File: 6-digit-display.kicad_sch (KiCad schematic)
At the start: 5 parts, among them U2 MAX7219, U3 6_digit_7_segment_display_1

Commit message: More footprint updates
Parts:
- U9: renamed from U3; footprint Generic-radio-stack:6 digit (3x2) 7 segment LED display -> Generic-radio-stack:6 digit (3+3) 7 segment LED display
- renumbered C4 to C10, C3 to C9, R10 to R13, U2 to U8
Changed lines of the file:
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@@
   (symbol (lib_id "Driver_LED:MAX7219") (at 60.96 101.6 0)
     (in_bom yes) (on_board yes) (fields_autoplaced)
-    (property "Reference" "U2" (id 0) (at 62.9794 73.66 0)
+    (property "Reference" "U8" (id 0) (at 62.9794 73.66 0)
       (effects (font (size 1.27 1.27)) (justify left))
     )
@@
   (symbol (lib_id "Device:C_Small") (at 38.1 78.74 0)
     (in_bom yes) (on_board yes) (fields_autoplaced)
-    (property "Reference" "C4" (id 0) (at 40.64 77.4762 0)
+    (property "Reference" "C10" (id 0) (at 40.64 77.4762 0)
       (effects (font (size 1.27 1.27)) (justify left))
     )
@@
   (symbol (lib_id "power:GND") (at 38.1 81.28 0)
     (in_bom yes) (on_board yes) (fields_autoplaced)
-    (property "Reference" "#PWR013" (id 0) (at 38.1 87.63 0)
+    (property "Reference" "#PWR025" (id 0) (at 38.1 87.63 0)
       (effects (font (size 1.27 1.27)) hide)
     )
@@
   (symbol (lib_id "Device:R_Small") (at 48.26 87.63 0)
     (in_bom yes) (on_board yes)
-    (property "Reference" "R10" (id 0) (at 46.99 86.36 0)
+    (property "Reference" "R13" (id 0) (at 46.99 86.36 0)
       (effects (font (size 1.27 1.27)) (justify right))
     )
@@
   (symbol (lib_id "power:+5V") (at 38.1 76.2 0)
     (in_bom yes) (on_board yes) (fields_autoplaced)
-    (property "Reference" "#PWR012" (id 0) (at 38.1 80.01 0)
+    (property "Reference" "#PWR024" (id 0) (at 38.1 80.01 0)
       (effects (font (size 1.27 1.27)) hide)
     )
@@
   (symbol (lib_id "power:GND") (at 48.26 90.17 0)
     (in_bom yes) (on_board yes) (fields_autoplaced)
-    (property "Reference" "#PWR014" (id 0) (at 48.26 96.52 0)
+    (property "Reference" "#PWR026" (id 0) (at 48.26 96.52 0)
       (effects (font (size 1.27 1.27)) hide)
     )
@@
   (symbol (lib_id "power:GND") (at 60.96 127 0)
     (in_bom yes) (on_board yes) (fields_autoplaced)
-    (property "Reference" "#PWR015" (id 0) (at 60.96 133.35 0)
+    (property "Reference" "#PWR027" (id 0) (at 60.96 133.35 0)
       (effects (font (size 1.27 1.27)) hide)
     )
@@
   (symbol (lib_id "Generic-radio-stack:6_digit_7_segment_display_1") (at 113.03 90.17 0)
     (in_bom yes) (on_board yes) (fields_autoplaced)
-    (property "Reference" "U3" (id 0) (at 114.3 74.93 0))
+    (property "Reference" "U9" (id 0) (at 114.3 74.93 0))
     (property "Value" "6_digit_7_segment_display_1" (id 1) (at 114.3 77.47 0))
-    (property "Footprint" "Generic-radio-stack:6 digit (3x2) 7 segment LED display" (id 2) (at 113.03 104.775 0)
+    (property "Footprint" "Generic-radio-stack:6 digit (3+3) 7 segment LED display" (id 2) (at 113.03 104.775 0)
       (effects (font (size 1.27 1.27)) hide)
     )
@@
   (symbol (lib_id "Device:C_Small") (at 27.94 78.74 0)
     (in_bom yes) (on_board yes) (fields_autoplaced)
-    (property "Reference" "C3" (id 0) (at 30.48 77.4762 0)
+    (property "Reference" "C9" (id 0) (at 30.48 77.4762 0)
       (effects (font (size 1.27 1.27)) (justify left))
     )

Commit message: Board layout begins. Ugh.
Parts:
- renumbered C9 to C7, C10 to C8, R13 to R12, U8 to U6, U9 to U7
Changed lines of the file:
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@@
   (symbol (lib_id "Driver_LED:MAX7219") (at 60.96 101.6 0)
     (in_bom yes) (on_board yes) (fields_autoplaced)
-    (property "Reference" "U8" (id 0) (at 62.9794 73.66 0)
+    (property "Reference" "U6" (id 0) (at 62.9794 73.66 0)
       (effects (font (size 1.27 1.27)) (justify left))
     )
@@
   (symbol (lib_id "Device:C_Small") (at 38.1 78.74 0)
     (in_bom yes) (on_board yes) (fields_autoplaced)
-    (property "Reference" "C10" (id 0) (at 40.64 77.4762 0)
+    (property "Reference" "C8" (id 0) (at 40.64 77.4762 0)
       (effects (font (size 1.27 1.27)) (justify left))
     )
@@
   (symbol (lib_id "power:GND") (at 38.1 81.28 0)
     (in_bom yes) (on_board yes) (fields_autoplaced)
-    (property "Reference" "#PWR025" (id 0) (at 38.1 87.63 0)
+    (property "Reference" "#PWR021" (id 0) (at 38.1 87.63 0)
       (effects (font (size 1.27 1.27)) hide)
     )
@@
   (symbol (lib_id "Device:R_Small") (at 48.26 87.63 0)
     (in_bom yes) (on_board yes)
-    (property "Reference" "R13" (id 0) (at 46.99 86.36 0)
+    (property "Reference" "R12" (id 0) (at 46.99 86.36 0)
       (effects (font (size 1.27 1.27)) (justify right))
     )
@@
   (symbol (lib_id "power:+5V") (at 38.1 76.2 0)
     (in_bom yes) (on_board yes) (fields_autoplaced)
-    (property "Reference" "#PWR024" (id 0) (at 38.1 80.01 0)
+    (property "Reference" "#PWR020" (id 0) (at 38.1 80.01 0)
       (effects (font (size 1.27 1.27)) hide)
     )
@@
   (symbol (lib_id "power:GND") (at 48.26 90.17 0)
     (in_bom yes) (on_board yes) (fields_autoplaced)
-    (property "Reference" "#PWR026" (id 0) (at 48.26 96.52 0)
+    (property "Reference" "#PWR022" (id 0) (at 48.26 96.52 0)
       (effects (font (size 1.27 1.27)) hide)
     )
@@
   (symbol (lib_id "power:GND") (at 60.96 127 0)
     (in_bom yes) (on_board yes) (fields_autoplaced)
-    (property "Reference" "#PWR027" (id 0) (at 60.96 133.35 0)
+    (property "Reference" "#PWR023" (id 0) (at 60.96 133.35 0)
       (effects (font (size 1.27 1.27)) hide)
     )
@@
   (symbol (lib_id "Generic-radio-stack:6_digit_7_segment_display_1") (at 113.03 90.17 0)
     (in_bom yes) (on_board yes) (fields_autoplaced)
-    (property "Reference" "U9" (id 0) (at 114.3 74.93 0))
+    (property "Reference" "U7" (id 0) (at 114.3 74.93 0))
     (property "Value" "6_digit_7_segment_display_1" (id 1) (at 114.3 77.47 0))
     (property "Footprint" "Generic-radio-stack:6 digit (3+3) 7 segment LED display" (id 2) (at 113.03 104.775 0)
@@
   (symbol (lib_id "Device:C_Small") (at 27.94 78.74 0)
     (in_bom yes) (on_board yes) (fields_autoplaced)
-    (property "Reference" "C9" (id 0) (at 30.48 77.4762 0)
+    (property "Reference" "C7" (id 0) (at 30.48 77.4762 0)
       (effects (font (size 1.27 1.27)) (justify left))
     )

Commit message: Added dual encoder 3d model, fit everything on the board
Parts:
- renumbered C8 to C10, C7 to C9, R12 to R13, U7 to U10, U6 to U9
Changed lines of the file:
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@@
   (symbol (lib_id "Driver_LED:MAX7219") (at 60.96 101.6 0)
     (in_bom yes) (on_board yes) (fields_autoplaced)
-    (property "Reference" "U6" (id 0) (at 62.9794 73.66 0)
+    (property "Reference" "U9" (id 0) (at 62.9794 73.66 0)
       (effects (font (size 1.27 1.27)) (justify left))
     )
@@
   (symbol (lib_id "Device:C_Small") (at 38.1 78.74 0)
     (in_bom yes) (on_board yes) (fields_autoplaced)
-    (property "Reference" "C8" (id 0) (at 40.64 77.4762 0)
+    (property "Reference" "C10" (id 0) (at 40.64 77.4762 0)
       (effects (font (size 1.27 1.27)) (justify left))
     )
@@
   (symbol (lib_id "power:GND") (at 38.1 81.28 0)
     (in_bom yes) (on_board yes) (fields_autoplaced)
-    (property "Reference" "#PWR021" (id 0) (at 38.1 87.63 0)
+    (property "Reference" "#PWR027" (id 0) (at 38.1 87.63 0)
       (effects (font (size 1.27 1.27)) hide)
     )
@@
   (symbol (lib_id "Device:R_Small") (at 48.26 87.63 0)
     (in_bom yes) (on_board yes)
-    (property "Reference" "R12" (id 0) (at 46.99 86.36 0)
+    (property "Reference" "R13" (id 0) (at 46.99 86.36 0)
       (effects (font (size 1.27 1.27)) (justify right))
     )
@@
   (symbol (lib_id "power:+5V") (at 38.1 76.2 0)
     (in_bom yes) (on_board yes) (fields_autoplaced)
-    (property "Reference" "#PWR020" (id 0) (at 38.1 80.01 0)
+    (property "Reference" "#PWR026" (id 0) (at 38.1 80.01 0)
       (effects (font (size 1.27 1.27)) hide)
     )
@@
   (symbol (lib_id "power:GND") (at 48.26 90.17 0)
     (in_bom yes) (on_board yes) (fields_autoplaced)
-    (property "Reference" "#PWR022" (id 0) (at 48.26 96.52 0)
+    (property "Reference" "#PWR028" (id 0) (at 48.26 96.52 0)
       (effects (font (size 1.27 1.27)) hide)
     )
@@
   (symbol (lib_id "power:GND") (at 60.96 127 0)
     (in_bom yes) (on_board yes) (fields_autoplaced)
-    (property "Reference" "#PWR023" (id 0) (at 60.96 133.35 0)
+    (property "Reference" "#PWR029" (id 0) (at 60.96 133.35 0)
       (effects (font (size 1.27 1.27)) hide)
     )
@@
   (symbol (lib_id "Generic-radio-stack:6_digit_7_segment_display_1") (at 113.03 90.17 0)
     (in_bom yes) (on_board yes) (fields_autoplaced)
-    (property "Reference" "U7" (id 0) (at 114.3 74.93 0))
+    (property "Reference" "U10" (id 0) (at 114.3 74.93 0))
     (property "Value" "6_digit_7_segment_display_1" (id 1) (at 114.3 77.47 0))
     (property "Footprint" "Generic-radio-stack:6 digit (3+3) 7 segment LED display" (id 2) (at 113.03 104.775 0)
@@
   (symbol (lib_id "Device:C_Small") (at 27.94 78.74 0)
     (in_bom yes) (on_board yes) (fields_autoplaced)
-    (property "Reference" "C7" (id 0) (at 30.48 77.4762 0)
+    (property "Reference" "C9" (id 0) (at 30.48 77.4762 0)
       (effects (font (size 1.27 1.27)) (justify left))
     )

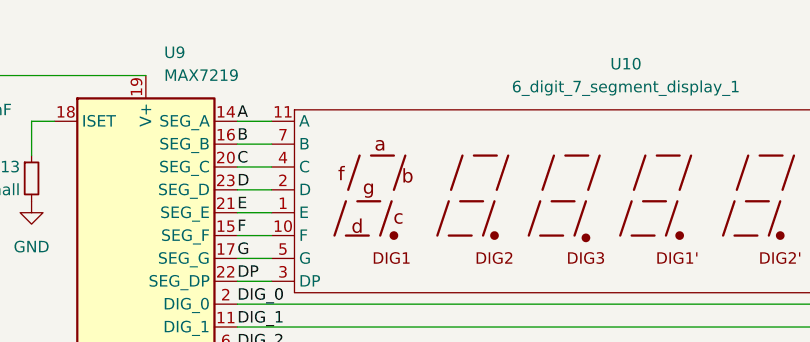
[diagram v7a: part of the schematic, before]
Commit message: Add mounting holes
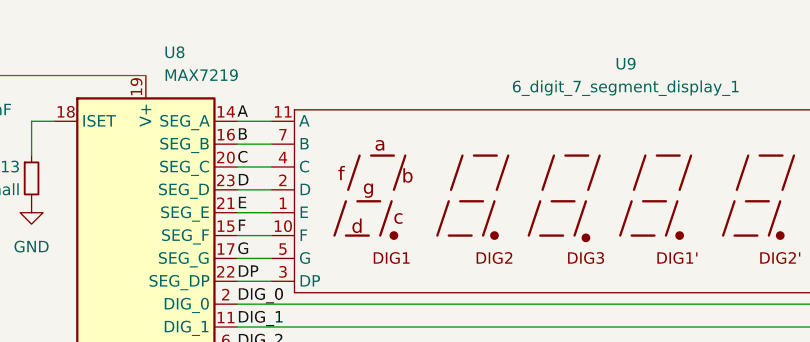
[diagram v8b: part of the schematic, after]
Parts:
- renumbered U9 to U8, U10 to U9
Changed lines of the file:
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@@
   (symbol (lib_id "Driver_LED:MAX7219") (at 60.96 101.6 0)
     (in_bom yes) (on_board yes) (fields_autoplaced)
-    (property "Reference" "U9" (id 0) (at 62.9794 73.66 0)
+    (property "Reference" "U8" (id 0) (at 62.9794 73.66 0)
       (effects (font (size 1.27 1.27)) (justify left))
     )
@@
   (symbol (lib_id "power:GND") (at 38.1 81.28 0)
     (in_bom yes) (on_board yes) (fields_autoplaced)
-    (property "Reference" "#PWR027" (id 0) (at 38.1 87.63 0)
+    (property "Reference" "#PWR025" (id 0) (at 38.1 87.63 0)
       (effects (font (size 1.27 1.27)) hide)
     )
@@
   (symbol (lib_id "power:+5V") (at 38.1 76.2 0)
     (in_bom yes) (on_board yes) (fields_autoplaced)
-    (property "Reference" "#PWR026" (id 0) (at 38.1 80.01 0)
+    (property "Reference" "#PWR024" (id 0) (at 38.1 80.01 0)
       (effects (font (size 1.27 1.27)) hide)
     )
@@
   (symbol (lib_id "power:GND") (at 48.26 90.17 0)
     (in_bom yes) (on_board yes) (fields_autoplaced)
-    (property "Reference" "#PWR028" (id 0) (at 48.26 96.52 0)
+    (property "Reference" "#PWR026" (id 0) (at 48.26 96.52 0)
       (effects (font (size 1.27 1.27)) hide)
     )
@@
   (symbol (lib_id "power:GND") (at 60.96 127 0)
     (in_bom yes) (on_board yes) (fields_autoplaced)
-    (property "Reference" "#PWR029" (id 0) (at 60.96 133.35 0)
+    (property "Reference" "#PWR027" (id 0) (at 60.96 133.35 0)
       (effects (font (size 1.27 1.27)) hide)
     )
@@
   (symbol (lib_id "Generic-radio-stack:6_digit_7_segment_display_1") (at 113.03 90.17 0)
     (in_bom yes) (on_board yes) (fields_autoplaced)
-    (property "Reference" "U10" (id 0) (at 114.3 74.93 0))
+    (property "Reference" "U9" (id 0) (at 114.3 74.93 0))
     (property "Value" "6_digit_7_segment_display_1" (id 1) (at 114.3 77.47 0))
     (property "Footprint" "Generic-radio-stack:6 digit (3+3) 7 segment LED display" (id 2) (at 113.03 104.775 0)
